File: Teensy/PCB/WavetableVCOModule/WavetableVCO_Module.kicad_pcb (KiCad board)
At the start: 2 copper layers, 55.9 x 101.6 mm, 33 parts, among them J1 Micro_SD_Card, J2 Power_Connector_2x3, SW1 Next_File_Button, U1 SPI_Oled, U2 Teensy4.0

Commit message: Generated Gerbers
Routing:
- net /T22: track 115.4 -> 110.2 mm
- net /T21: track 89.7 -> 90.3 mm
- net /T12: track 22.0 -> 22.6 mm
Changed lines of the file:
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@@
       (layerselection 0x00010fc_ffffffff)
       (disableapertmacros false)
-      (usegerberextensions false)
-      (usegerberattributes true)
-      (usegerberadvancedattributes true)
-      (creategerberjobfile true)
+      (usegerberextensions true)
+      (usegerberattributes false)
+      (usegerberadvancedattributes false)
+      (creategerberjobfile false)
       (svguseinch false)
       (svgprecision 6)
@@
       (psa4output false)
       (plotreference true)
-      (plotvalue true)
+      (plotvalue false)
       (plotinvisibletext false)
       (sketchpadsonfab false)
-      (subtractmaskfromsilk false)
+      (subtractmaskfromsilk true)
       (outputformat 1)
       (mirror false)
-      (drillshape 1)
+      (drillshape 0)
       (scaleselection 1)
-      (outputdirectory "")
+      (outputdirectory "WavetableVCO_Module_Gerbers/")
     )
   )
@@
   (gr_rect (start 63.5 172.72) (end 119.38 71.12) (layer "Edge.Cuts") (width 0.1) (fill none))
   (gr_text "+" (at 109.22 154.94) (layer "B.SilkS")
-    (effects (font (size 1.5 1.5) (thickness 0.3)))
+    (effects (font (size 2 2) (thickness 0.3)))
   )
   (segment (start 112.776 154.94) (end 116.078 151.638) (width 0.25) (layer "F.Cu") (net 1))
@@
   (segment (start 102.734 79.13) (end 102.734 79.112) (width 0.25) (layer "B.Cu") (net 13))
   (segment (start 112.014 85.344) (end 106.68 90.678) (width 0.25) (layer "B.Cu") (net 13))
-  (segment (start 106.648 76.93) (end 109.728 80.01) (width 0.25) (layer "B.Cu") (net 14))
+  (segment (start 107.664 76.93) (end 109.728 78.994) (width 0.25) (layer "B.Cu") (net 14))
+  (segment (start 109.728 82.042) (end 105.918 85.852) (width 0.25) (layer "B.Cu") (net 14))
   (segment (start 105.918 85.852) (end 101.808 85.852) (width 0.25) (layer "B.Cu") (net 14))
-  (segment (start 109.728 80.01) (end 109.728 82.042) (width 0.25) (layer "B.Cu") (net 14))
-  (segment (start 109.728 82.042) (end 105.918 85.852) (width 0.25) (layer "B.Cu") (net 14))
   (segment (start 101.808 85.852) (end 98.76 88.9) (width 0.25) (layer "B.Cu") (net 14))
-  (segment (start 104.86 76.93) (end 106.648 76.93) (width 0.25) (layer "B.Cu") (net 14))
+  (segment (start 104.86 76.93) (end 107.664 76.93) (width 0.25) (layer "B.Cu") (net 14))
+  (segment (start 109.728 78.994) (end 109.728 82.042) (width 0.25) (layer "B.Cu") (net 14))
   (segment (start 110.21 164.82) (end 102.616 157.226) (width 0.25) (layer "B.Cu") (net 17))
   (segment (start 102.616 157.226) (end 83.947 157.226) (width 0.25) (layer "B.Cu") (net 17))
@@
   (segment (start 80.518 101.6) (end 80.518 94.234) (width 0.25) (layer "B.Cu") (net 21))
   (segment (start 86.568 93.472) (end 91.14 88.9) (width 0.25) (layer "B.Cu") (net 21))
-  (segment (start 102.108 105.41) (end 106.426 101.092) (width 0.25) (layer "F.Cu") (net 22))
+  (segment (start 71.08 139.7) (end 73.112 141.732) (width 0.25) (layer "F.Cu") (net 22))
+  (segment (start 106.426 101.092) (end 106.426 92.456) (width 0.25) (layer "F.Cu") (net 22))
+  (segment (start 84.582 84.836) (end 73.406 73.66) (width 0.25) (layer "F.Cu") (net 22))
+  (segment (start 102.362 123.444) (end 102.362 105.156) (width 0.25) (layer "F.Cu") (net 22))
   (segment (start 73.406 73.66) (end 73.36 73.66) (width 0.25) (layer "F.Cu") (net 22))
   (segment (start 106.426 92.456) (end 98.806 84.836) (width 0.25) (layer "F.Cu") (net 22))
-  (segment (start 71.08 139.7) (end 73.112 141.732) (width 0.25) (layer "F.Cu") (net 22))
-  (segment (start 106.426 101.092) (end 106.426 92.456) (width 0.25) (layer "F.Cu") (net 22))
-  (segment (start 102.108 123.698) (end 102.108 105.41) (width 0.25) (layer "F.Cu") (net 22))
-  (segment (start 84.582 84.836) (end 73.406 73.66) (width 0.25) (layer "F.Cu") (net 22))
   (segment (start 73.112 141.732) (end 84.074 141.732) (width 0.25) (layer "F.Cu") (net 22))
-  (segment (start 84.074 141.732) (end 102.108 123.698) (width 0.25) (layer "F.Cu") (net 22))
+  (segment (start 84.074 141.732) (end 102.362 123.444) (width 0.25) (layer "F.Cu") (net 22))
+  (segment (start 102.362 105.156) (end 106.426 101.092) (width 0.25) (layer "F.Cu") (net 22))
   (segment (start 98.806 84.836) (end 84.582 84.836) (width 0.25) (layer "F.Cu") (net 22))
   (segment (start 85.09 102.108) (end 80.264 102.108) (width 0.25) (layer "F.Cu") (net 23))
@@
   (segment (start 78.232 125.476) (end 80.772 122.936) (width 0.25) (layer "B.Cu") (net 25))
   (segment (start 80.772 104.648) (end 78.232 102.108) (width 0.25) (layer "B.Cu") (net 25))
-  (segment (start 105.918 144.526) (end 105.918 139.446) (width 0.25) (layer "F.Cu") (net 26))
-  (segment (start 104.648 121.666) (end 104.648 111.76) (width 0.25) (layer "F.Cu") (net 26))
-  (segment (start 109.982 135.382) (end 109.982 127) (width 0.25) (layer "F.Cu") (net 26))
   (segment (start 91.485 152.415) (end 91.485 151.085) (width 0.25) (layer "F.Cu") (net 26))
-  (segment (start 93.472 149.098) (end 101.346 149.098) (width 0.25) (layer "F.Cu") (net 26))
   (segment (start 75.946 73.66) (end 75.9 73.66) (width 0.25) (layer "F.Cu") (net 26))
-  (segment (start 105.918 139.446) (end 109.982 135.382) (width 0.25) (layer "F.Cu") (net 26))
-  (segment (start 109.982 127) (end 104.648 121.666) (width 0.25) (layer "F.Cu") (net 26))
-  (segment (start 104.648 111.76) (end 107.442 108.966) (width 0.25) (layer "F.Cu") (net 26))
-  (segment (start 107.442 108.966) (end 107.442 91.694) (width 0.25) (layer "F.Cu") (net 26))
-  (segment (start 91.485 151.085) (end 93.472 149.098) (width 0.25) (layer "F.Cu") (net 26))
-  (segment (start 101.346 149.098) (end 105.918 144.526) (width 0.25) (layer "F.Cu") (net 26))
+  (segment (start 101.854 137.414) (end 103.378 135.89) (width 0.25) (layer "F.Cu") (net 26))
+  (segment (start 107.442 108.458) (end 107.442 91.694) (width 0.25) (layer "F.Cu") (net 26))
   (segment (start 86.106 83.82) (end 75.946 73.66) (width 0.25) (layer "F.Cu") (net 26))
   (segment (start 99.568 83.82) (end 86.106 83.82) (width 0.25) (layer "F.Cu") (net 26))
   (segment (start 107.442 91.694) (end 99.568 83.82) (width 0.25) (layer "F.Cu") (net 26))
+  (segment (start 103.378 112.522) (end 107.442 108.458) (width 0.25) (layer "F.Cu") (net 26))
+  (segment (start 101.854 147.32) (end 101.854 137.414) (width 0.25) (layer "F.Cu") (net 26))
+  (segment (start 103.378 135.89) (end 103.378 112.522) (width 0.25) (layer "F.Cu") (net 26))
+  (segment (start 93.472 149.098) (end 100.076 149.098) (width 0.25) (layer "F.Cu") (net 26))
+  (segment (start 100.076 149.098) (end 101.854 147.32) (width 0.25) (layer "F.Cu") (net 26))
+  (segment (start 91.485 151.085) (end 93.472 149.098) (width 0.25) (layer "F.Cu") (net 26))
   (segment (start 73.36 96.982) (end 73.36 88.9) (width 0.25) (layer "F.Cu") (net 27))
   (segment (start 86.36 105.156) (end 81.534 105.156) (width 0.25) (layer "F.Cu") (net 27))
@@
   (segment (start 82.804 127.508) (end 83.82 126.492) (width 0.25) (layer "B.Cu") (net 29))
   (segment (start 89.916 142.494) (end 82.042 134.62) (width 0.25) (layer "B.Cu") (net 29))
+  (segment (start 108.458 109.22) (end 108.458 91.186) (width 0.25) (layer "F.Cu") (net 30))
+  (segment (start 99.568 82.296) (end 87.076 82.296) (width 0.25) (layer "F.Cu") (net 30))
+  (segment (start 87.076 82.296) (end 78.44 73.66) (width 0.25) (layer "F.Cu") (net 30))
+  (segment (start 104.648 113.03) (end 108.458 109.22) (width 0.25) (layer "F.Cu") (net 30))
+  (segment (start 110.998 126.238) (end 104.648 119.888) (width 0.25) (layer "F.Cu") (net 30))
   (segment (start 111.76 139.7) (end 111.76 136.144) (width 0.25) (layer "F.Cu") (net 30))
-  (segment (start 110.998 126.238) (end 105.41 120.65) (width 0.25) (layer "F.Cu") (net 30))
+  (segment (start 111.76 136.144) (end 110.998 135.382) (width 0.25) (layer "F.Cu") (net 30))
+  (segment (start 108.458 91.186) (end 99.568 82.296) (width 0.25) (layer "F.Cu") (net 30))
   (segment (start 110.998 135.382) (end 110.998 126.238) (width 0.25) (layer "F.Cu") (net 30))
-  (segment (start 108.458 91.186) (end 99.568 82.296) (width 0.25) (layer "F.Cu") (net 30))
-  (segment (start 105.41 112.268) (end 108.458 109.22) (width 0.25) (layer "F.Cu") (net 30))
-  (segment (start 105.41 120.65) (end 105.41 112.268) (width 0.25) (layer "F.Cu") (net 30))
-  (segment (start 111.76 136.144) (end 110.998 135.382) (width 0.25) (layer "F.Cu") (net 30))
-  (segment (start 87.076 82.296) (end 78.44 73.66) (width 0.25) (layer "F.Cu") (net 30))
-  (segment (start 99.568 82.296) (end 87.076 82.296) (width 0.25) (layer "F.Cu") (net 30))
-  (segment (start 108.458 109.22) (end 108.458 91.186) (width 0.25) (layer "F.Cu") (net 30))
+  (segment (start 104.648 119.888) (end 104.648 113.03) (width 0.25) (layer "F.Cu") (net 30))
   (segment (start 88.6 88.946) (end 88.6 88.9) (width 0.25) (layer "F.Cu") (net 31))
   (segment (start 85.09 92.456) (end 88.6 88.946) (width 0.25) (layer "F.Cu") (net 31))

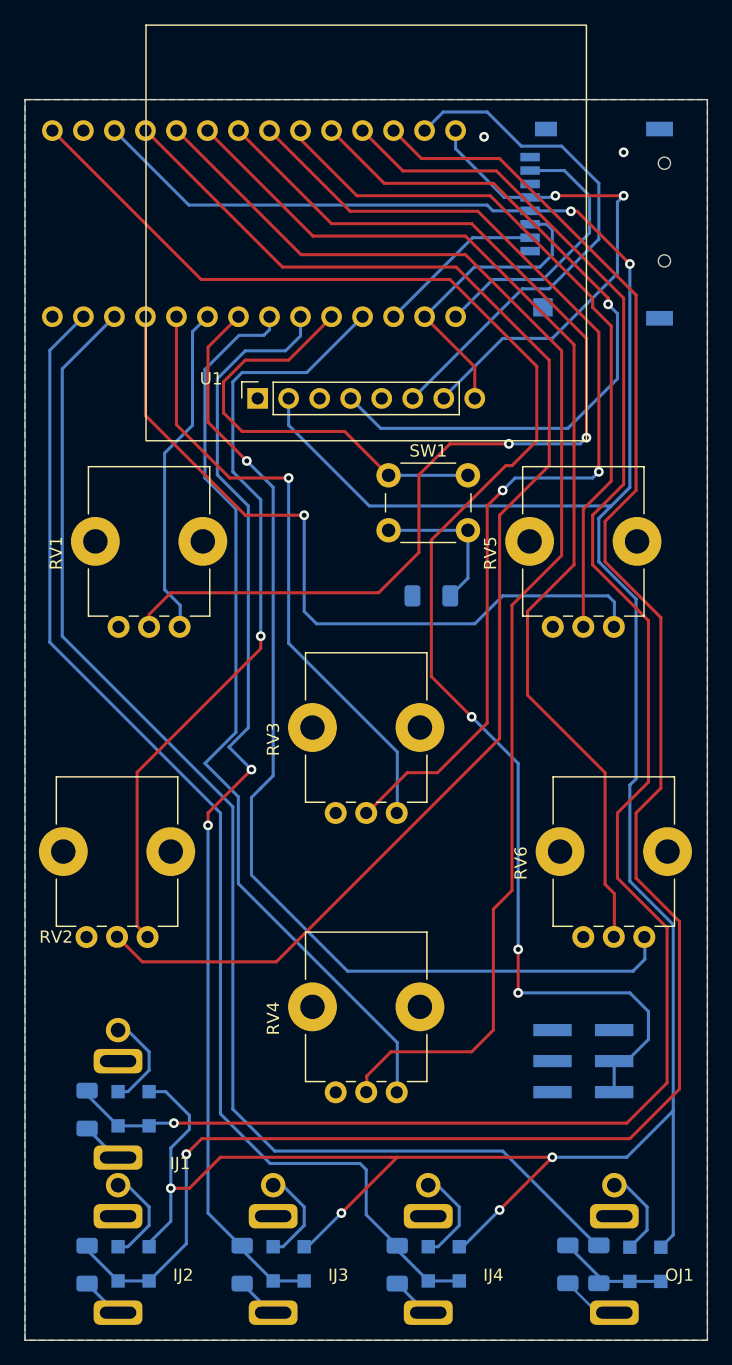
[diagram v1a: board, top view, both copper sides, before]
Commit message: Made NPTH holes 0.5mm bigger; adjusted diode pads for better solderability
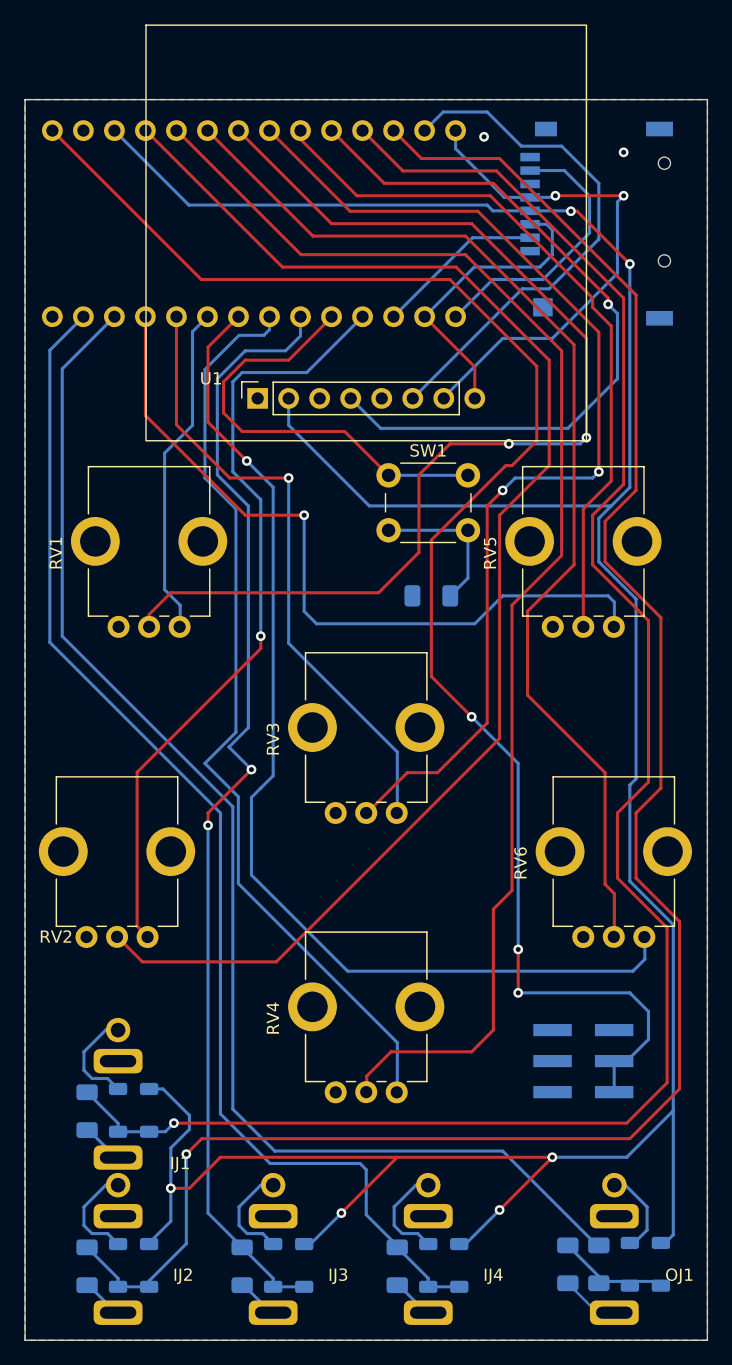
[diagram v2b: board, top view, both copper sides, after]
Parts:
- ID1, ID2, ID3, ID4, ID5, ID6, ID7, ID8, OD1, OD2: footprint Diode_SMD:D_SOD-123F -> Misc:D_SOD-123 Handsolder
- moved ID1 0.13 mm to (71.1, 153.9)
- moved ID2 0.13 mm to (73.7, 153.9)
- moved ID3 0.13 mm to (71.1, 166.6)
- moved ID4 0.13 mm to (73.7, 166.6)
- moved ID5 0.13 mm to (83.8, 166.6)
- moved ID6 0.13 mm to (86.4, 166.6)
- moved ID7 0.13 mm to (96.5, 166.6)
- moved ID8 0.13 mm to (99.1, 166.6)
- moved IR1 0.13 mm to (68.6, 154.0)
- moved IR2 0.13 mm to (68.6, 166.7)
- moved IR3 0.13 mm to (81.3, 166.7)
- moved IR4 0.13 mm to (94.0, 166.7)
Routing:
- net GND: track 39.6 -> 41.2 mm
- net /T15: track 156.4 -> 157.3 mm
- net /T16: track 147.4 -> 147.9 mm

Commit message: Added USB-C Power Supply
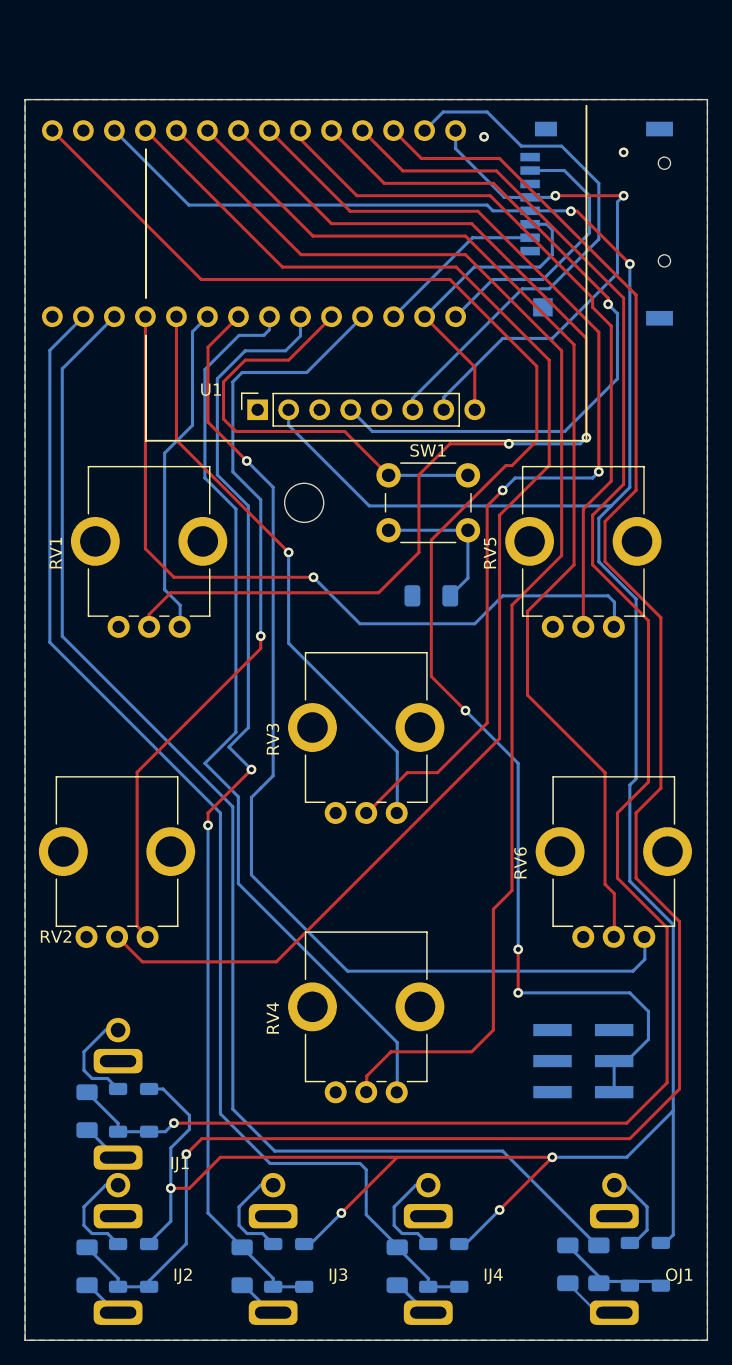
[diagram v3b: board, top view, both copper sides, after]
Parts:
- added REF**: MountingHole_3.2mm_M3_DIN965, MountingHole:MountingHole_3.2mm_M3_DIN965, F.Cu at (86.4, 104.1)
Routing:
- net /T3: track 51.0 -> 48.1 mm
- net /T2: track 61.4 -> 63.2 mm
- net /T14: track 42.5 -> 43.5 mm
- net /T13: track 42.0 -> 43.0 mm
- net /T11: track 25.0 -> 25.9 mm
- net +3.3V: track 244.2 -> 243.3 mm
